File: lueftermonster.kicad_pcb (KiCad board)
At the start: 2 copper layers, 87 parts, among them J1 Barrel_Jack, J10 Fan, J11 Fan, J12 Fan, J13 Fan, J14 Fan, J15 Fan, J16 Fan, J17 PROG, J2 Fan, J3 Fan, J4 Fan, J5 Fan, J6 Fan, J7 Fan, J8 Fan, J9 Fan, Q1 Q_PMOS_GSD, Q2 Q_NMOS_GSD, Q3 Q_NMOS_GSD, Q4 Q_NMOS_GSD, Q5 Q_NMOS_GSD, U1 ESP32-WROOM-32E, U2 AOZ1280CI, U3 AMS1117-5.0

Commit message: bullshit placing to make gerbers sane
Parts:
- C1, C3: value TBD -> 100n; footprint Capacitor_SMD:C_0402_1005Metric -> Capacitor_SMD:C_0805_2012Metric
- C6, C7: footprint Capacitor_SMD:C_0805_2012Metric -> Capacitor_SMD:C_1206_3216Metric
- FB1, FB2: value 30R @ 100MHz -> 120R @ 100MHz; footprint Inductor_SMD:L_0603_1608Metric -> Inductor_SMD:L_1206_3216Metric
- moved FB2 189.7 mm to (134.2, 114.7)
- moved FB1 189.3 mm to (134.2, 111.2)
- moved C3 186.7 mm to (139.3, 114.0)
- moved C1 186.4 mm to (139.3, 111.0)
- moved C5 173.9 mm to (121.4, 107.3)
- moved F1 173.9 mm to (100.2, 95.5)
- moved D1 173.9 mm to (99.6, 114.5)
- moved J1 173.9 mm to (112.3, 107.0)
- moved Q1 173.9 mm to (120.5, 115.7)
- moved R1 173.9 mm to (99.3, 116.8)
- moved J14 172.6 mm to (207.9, 65.2)
- moved J15 172.6 mm to (207.9, 73.3)
- moved J16 172.6 mm to (207.9, 81.3)
- moved J10 166.1 mm to (193.7, 65.2)
- moved J11 166.1 mm to (193.7, 73.2)
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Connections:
- FB1 pad 1: +12V -> Net-(C1-Pad1)
- FB1 pad 2: Net-(C1-Pad1) -> +12V
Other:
- board outline added: 130 x 60 mm

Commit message: snap
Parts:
- added H1: MountingHole_Pad, MountingHole:MountingHole_3.2mm_M3_ISO14580_Pad, F.Cu at (101.3, 64.4)
- added H2: MountingHole_Pad, MountingHole:MountingHole_3.2mm_M3_ISO14580_Pad, F.Cu at (223.3, 64.4)
- added H3: MountingHole_Pad, MountingHole:MountingHole_3.2mm_M3_ISO14580_Pad, F.Cu at (223.3, 116.4)
- added H4: MountingHole_Pad, MountingHole:MountingHole_3.2mm_M3_ISO14580_Pad, F.Cu at (101.3, 116.4)
- moved J17 120.8 mm to (222.1, 103.5)
- moved R6 119.9 mm to (270.5, 127.1)
- moved Q2 119.9 mm to (267.1, 123.9)
- moved Q3 119.9 mm to (267.4, 131.7)
- moved Q4 119.9 mm to (267.4, 139.5)
- moved Q5 119.9 mm to (267.2, 147.6)
- moved R9 119.9 mm to (270.6, 150.8)
- moved R12 119.9 mm to (266.8, 127.4)
- moved R13 119.9 mm to (267.1, 135.2)
- moved R14 119.9 mm to (267.1, 142.9)
- moved R15 119.9 mm to (267.0, 151.0)
- moved R7 119.9 mm to (270.7, 134.9)
- moved R8 119.9 mm to (270.8, 142.7)
- moved R16 118.8 mm to (304.1, 102.1)
- moved R17 118.8 mm to (304.1, 104.1)
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
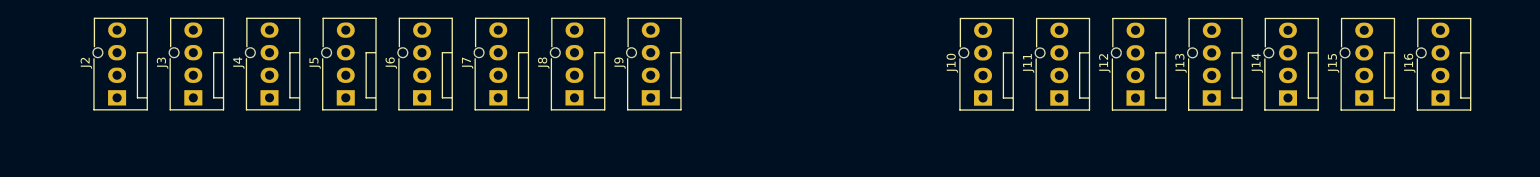
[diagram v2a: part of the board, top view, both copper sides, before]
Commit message: use 100mil headers for fans
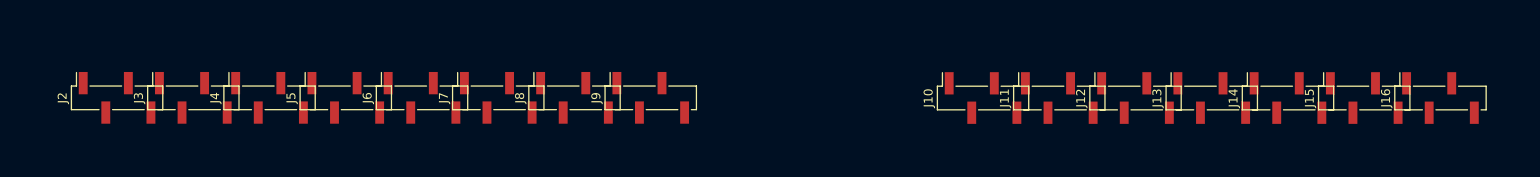
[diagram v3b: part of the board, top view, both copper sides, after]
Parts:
- J10, J11, J12, J13, J14, J15, J16, J2, J3, J4, J5, J6, J7, J8, J9: footprint Connector:FanPinHeader_1x04_P2.54mm_Vertical -> Connector_PinHeader_2.54mm:PinHeader_1x04_P2.54mm_Vertical_SMD_Pin1Right

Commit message: snap
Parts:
- removed C26: 10u, Capacitor_SMD:C_0805_2012Metric
- removed Q5: Q_NMOS_GSD, Package_TO_SOT_SMD:SOT-23
- added J18: W1, Connector_PinHeader_2.54mm:PinHeader_1x03_P2.54mm_Vertical_SMD_Pin1Left, F.Cu at (104.6, 92.1)
- added J19: W1, Connector_PinHeader_2.54mm:PinHeader_1x03_P2.54mm_Vertical_SMD_Pin1Left, F.Cu at (111.6, 92.1)
- added J20: W1, Connector_PinHeader_2.54mm:PinHeader_1x03_P2.54mm_Vertical_SMD_Pin1Left, F.Cu at (118.6, 92.1)
- added J21: W1, Connector_PinHeader_2.54mm:PinHeader_1x03_P2.54mm_Vertical_SMD_Pin1Left, F.Cu at (125.6, 92.1)
- added R31: 10k, Resistor_SMD:R_0402_1005Metric, F.Cu at (146.3, 117.1)
- added R32: 0R, Resistor_SMD:R_0603_1608Metric_Pad0.98x0.95mm_HandSolder, F.Cu at (102.8, 86.9)
- added R33: 10k, Resistor_SMD:R_0402_1005Metric, F.Cu at (108.9, 68.0)
- C4: value 100n -> 10n
- L1: footprint Inductor_SMD:L_Taiyo-Yuden_NR-24xx -> Inductor_SMD:L_1008_2520Metric
- R12, R13: value 1k -> 0R
- R14, R15: value 1k -> 10k; footprint Resistor_SMD:R_0603_1608Metric_Pad0.98x0.95mm_HandSolder -> Resistor_SMD:R_0402_1005Metric
- R9: value 1R -> TBD
- moved R30 199.3 mm to (112.0, 83.4), turned to 180 degrees
- moved R29 199.2 mm to (112.0, 82.1), turned to 180 degrees
- moved R28 199.1 mm to (112.0, 80.8), turned to 180 degrees
- moved R27 197.7 mm to (112.0, 79.6), turned to 180 degrees
- moved R26 197.6 mm to (112.0, 78.3), turned to 180 degrees
- moved R25 197.5 mm to (112.0, 77.0), turned to 180 degrees
- moved R24 197.4 mm to (112.0, 75.8), turned to 180 degrees
- moved R23 197.3 mm to (112.0, 74.5), turned to 180 degrees
- moved R22 174.6 mm to (133.6, 82.1)
- moved R17 173.7 mm to (133.6, 70.7)
- moved R16 173.6 mm to (133.6, 69.5)
- moved R21 173.3 mm to (133.6, 80.9)
- moved R20 173.2 mm to (133.8, 78.3)
- moved R18 173.2 mm to (133.8, 74.5)
- moved R19 173.1 mm to (133.8, 77.1)
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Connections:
- C4 pad 1: +3V3 -> /EN
- J10 pad 3: /TACH9 -> /TACH11
- J11 pad 3: /TACH10 -> /TACH12
- J12 pad 3: /TACH11 -> /TACH13
- J13 pad 3: /TACH12 -> /TACH14
- J14 pad 3: /TACH13 -> /TACH5
- J14 pad 4: /PWM_G4 -> /PWM_G1
- J15 pad 3: /TACH14 -> /TACH10
- J15 pad 4: /PWM_G4 -> /PWM_G2
- J16 pad 4: /PWM_G4 -> /PWM_G3
- J6 pad 3: /TACH5 -> /TACH6
- J7 pad 3: /TACH6 -> /TACH7
- J8 pad 3: /TACH7 -> /TACH8
- J9 pad 3: /TACH8 -> /TACH9
- R12 pad 1: /PWM_PU -> +5V
- R12 pad 2: /PWM_G1 -> /W1_SUPPLY
- R13 pad 1: /PWM_PU -> +12V
- R13 pad 2: /PWM_G2 -> /PWM_PU
- R14 pad 2: /PWM_G3 -> /PWM_G1
- R15 pad 2: /PWM_G4 -> /PWM_G2
- R9 pad 1: /PWM -> +3V3
- R9 pad 2: Net-(Q5-G) -> /W1
- U1 pad 10: /TACH9 -> /TACH12
- U1 pad 11: /TACH10 -> /TACH13
- U1 pad 12: /TACH11 -> /TACH14
- U1 pad 13: /TACH1 -> /TACH15
- U1 pad 26: unconnected-(U1-IO4-Pad26) -> /W1
- U1 pad 27: /TACH2 -> /TACH7
- U1 pad 28: /TACH3 -> /TACH6
- U1 pad 30: /TACH4 -> /TACH5
- U1 pad 31: /TACH5 -> /TACH4
- U1 pad 33: /TACH6 -> /TACH3
- U1 pad 36: /TACH7 -> /TACH2
- U1 pad 37: /TACH8 -> /TACH1
- U1 pad 6: /TACH14 -> /TACH8
- U1 pad 7: /TACH15 -> /TACH9
- U1 pad 8: /TACH12 -> /TACH10
- U1 pad 9: /TACH13 -> /TACH11
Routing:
- net +12V: track 0.00 -> 240.7 mm
- net +3V3: track 0.00 -> 85.9 mm
- net /TACH10: track 0.00 -> 35.3 mm
- net /TACH15: track 0.00 -> 35.0 mm
- net /TACH5: track 0.00 -> 33.6 mm
- net /PWM_G3: track 0.00 -> 31.0 mm
- net /PWM_G1: track 0.00 -> 30.9 mm
- net /PWM_G2: track 0.00 -> 30.9 mm
- net /W1_SUPPLY: track 0.00 -> 29.6 mm
- net /TACH9: track 0.00 -> 28.1 mm
- net /TACH14: track 0.00 -> 28.0 mm
- net /TACH4: track 0.00 -> 25.7 mm
- net /W1: track 0.00 -> 23.6 mm
- net /TACH8: track 0.00 -> 20.8 mm
- net /TACH13: track 0.00 -> 20.7 mm
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- added copper zone on B.Cu, net GND
- added copper zone on F.Cu, net GND
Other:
- board size 130 x 60 mm -> 94 x 60 mm
- board text added: "1"
- board text added: "12V"
- board text added: "GND"
- board text added: "PWM"
- board text added: "TACHO"
- board text added: "VCC"
- board text added: "W1"

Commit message: snap
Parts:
- moved R5 29.6 mm to (134.4, 68.7), turned to 90 degrees
- moved R26 5.08 mm to (112.0, 83.4)
- moved R30 5.08 mm to (112.0, 78.3)
- moved C8 4.18 mm to (136.4, 85.8)
- moved R17 3.80 mm to (133.7, 74.5)
- moved Q1 3.26 mm to (117.0, 105.9)
- moved R20 2.65 mm to (133.8, 81.0)
- moved C4 2.56 mm to (109.4, 68.5), turned to 90 degrees
- moved R27 2.54 mm to (112.0, 82.1)
- moved R29 2.54 mm to (112.0, 79.6)
- moved R18 2.50 mm to (133.8, 77.0)
- moved R33 2.50 mm to (109.4, 70.4), turned to 90 degrees
- moved D1 2.40 mm to (113.0, 104.3), turned to 90 degrees
- moved C7 2.08 mm to (141.3, 89.7)
- moved R10 2.08 mm to (139.2, 78.1)
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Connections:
- U1 pad 10: /TACH12 -> /TACH14
- U1 pad 12: /TACH14 -> /TACH12
- U1 pad 13: /TACH15 -> /TACH11
- U1 pad 16: /PWM -> /W1
- U1 pad 26: /W1 -> /TACH7
- U1 pad 27: /TACH7 -> /TACH6
- U1 pad 28: /TACH6 -> /TACH5
- U1 pad 30: /TACH5 -> /TACH4
- U1 pad 31: /TACH4 -> /TACH3
- U1 pad 33: /TACH3 -> /TACH2
- U1 pad 36: /TACH2 -> /TACH1
- U1 pad 37: /TACH1 -> /PWM
- U1 pad 9: /TACH11 -> /TACH15
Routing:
- net +12V: track 240.7 -> 284.3 mm
- net /RXD: track 0.00 -> 32.5 mm, vias 0 -> 2
- net /TACH11: track 5.96 -> 37.3 mm, vias 0 -> 3
- net /TACH13: track 20.7 -> 50.3 mm, vias 0 -> 3
- net /TACH12: track 13.7 -> 43.1 mm, vias 0 -> 3
- net Net-(D1-A1): track 0.00 -> 29.2 mm
- net /TXD: track 0.00 -> 28.5 mm, vias 0 -> 2
- net /TACH15: track 35.0 -> 62.8 mm, vias 0 -> 3
- net /TACH14: track 28.0 -> 55.4 mm, vias 0 -> 3
- net Net-(D1-A2): track 0.00 -> 25.8 mm
- net +5V: track 0.00 -> 19.1 mm
- net /IO0: track 0.00 -> 17.1 mm, vias 0 -> 2
- net /TACH7: track 11.5 -> 26.2 mm
- net /TACH6: track 3.75 -> 17.8 mm
- net /TACH8: track 20.8 -> 33.8 mm
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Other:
- board text added: "10"
- board text added: "11"
- board text added: "12"
- board text added: "13"
- board text added: "14"
- board text added: "15"
- board text added: "2"
- board text added: "3"
- board text added: "3v3"
- board text added: "4"
- board text added: "5"
- board text added: "6"
- board text added: "7"
- board text added: "8"
- board text added: "9"
- board text added: "EN"
- board text added: "IO0"
- board text added: "JLCJLCJLCJLC"
- board text added: "RXD"
- board text added: "TXD"

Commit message: 0 nets
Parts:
- moved R20 6.28 mm to (137.2, 75.7)
- moved R19 4.99 mm to (137.2, 74.7)
- moved R18 4.77 mm to (137.2, 73.7)
- moved R31 4.46 mm to (146.3, 112.6), turned to 180 degrees
- moved R17 3.98 mm to (137.2, 72.7)
- moved R13 3.85 mm to (141.2, 74.0), turned to -90 degrees
- moved R16 3.70 mm to (137.2, 71.7)
- moved R10 2.11 mm to (141.2, 77.4), turned to 90 degrees
- moved R11 1.82 mm to (139.1, 74.0), turned to -90 degrees
- moved R5 0.49 mm to (134.0, 68.9)
- moved R7 0.46 mm to (143.9, 94.3)
- moved R6 0.46 mm to (143.9, 74.4)
- moved R8 0.46 mm to (143.8, 114.4), turned to -90 degrees
- moved R21 0.24 mm to (134.0, 82.1)
- moved R22 0.21 mm to (134.0, 83.4)
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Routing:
- net /PWM: track 0.00 -> 59.5 mm, vias 0 -> 7
- net /PWM_PU: track 0.00 -> 46.3 mm, vias 0 -> 5
- net +3V3: track 97.6 -> 140.5 mm, vias 0 -> 2
- net /TACH9: track 40.6 -> 71.9 mm, vias 0 -> 2
- net /TACH8: track 33.8 -> 65.1 mm, vias 0 -> 2
- net /TACH10: track 47.6 -> 78.8 mm, vias 0 -> 2
- net /TACH14: track 55.4 -> 82.8 mm, vias 3 -> 4
- net /TACH15: track 62.8 -> 90.2 mm, vias 3 -> 4
- net /TACH13: track 50.3 -> 75.8 mm, vias 3 -> 4
- net /TACH12: track 43.1 -> 68.3 mm, vias 3 -> 4
- net /TACH11: track 37.3 -> 61.1 mm, vias 3 -> 4
- net /TACH5: track 33.6 -> 56.9 mm, vias 0 -> 2
- net /TACH3: track 18.2 -> 40.5 mm, vias 0 -> 2
- net /TACH4: track 25.7 -> 47.9 mm, vias 0 -> 2
- net /TACH2: track 10.6 -> 32.6 mm, vias 0 -> 2
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- added copper zone on F.Cu, net Net-(D2-K)
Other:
- board text added: "lueftermonster v1 2024-10-13"

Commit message: DRC clean
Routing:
- net +3V3: track 140.5 -> 139.4 mm
- net GND: vias 49 -> 137
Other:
- board text added: "TACH"
- board text removed: "TACHO"

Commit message: stitch
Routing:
- net GND: vias 137 -> 187
